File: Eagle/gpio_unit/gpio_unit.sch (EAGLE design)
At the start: 11 parts, among them X1 RASPI_GPIO_B+_PIN

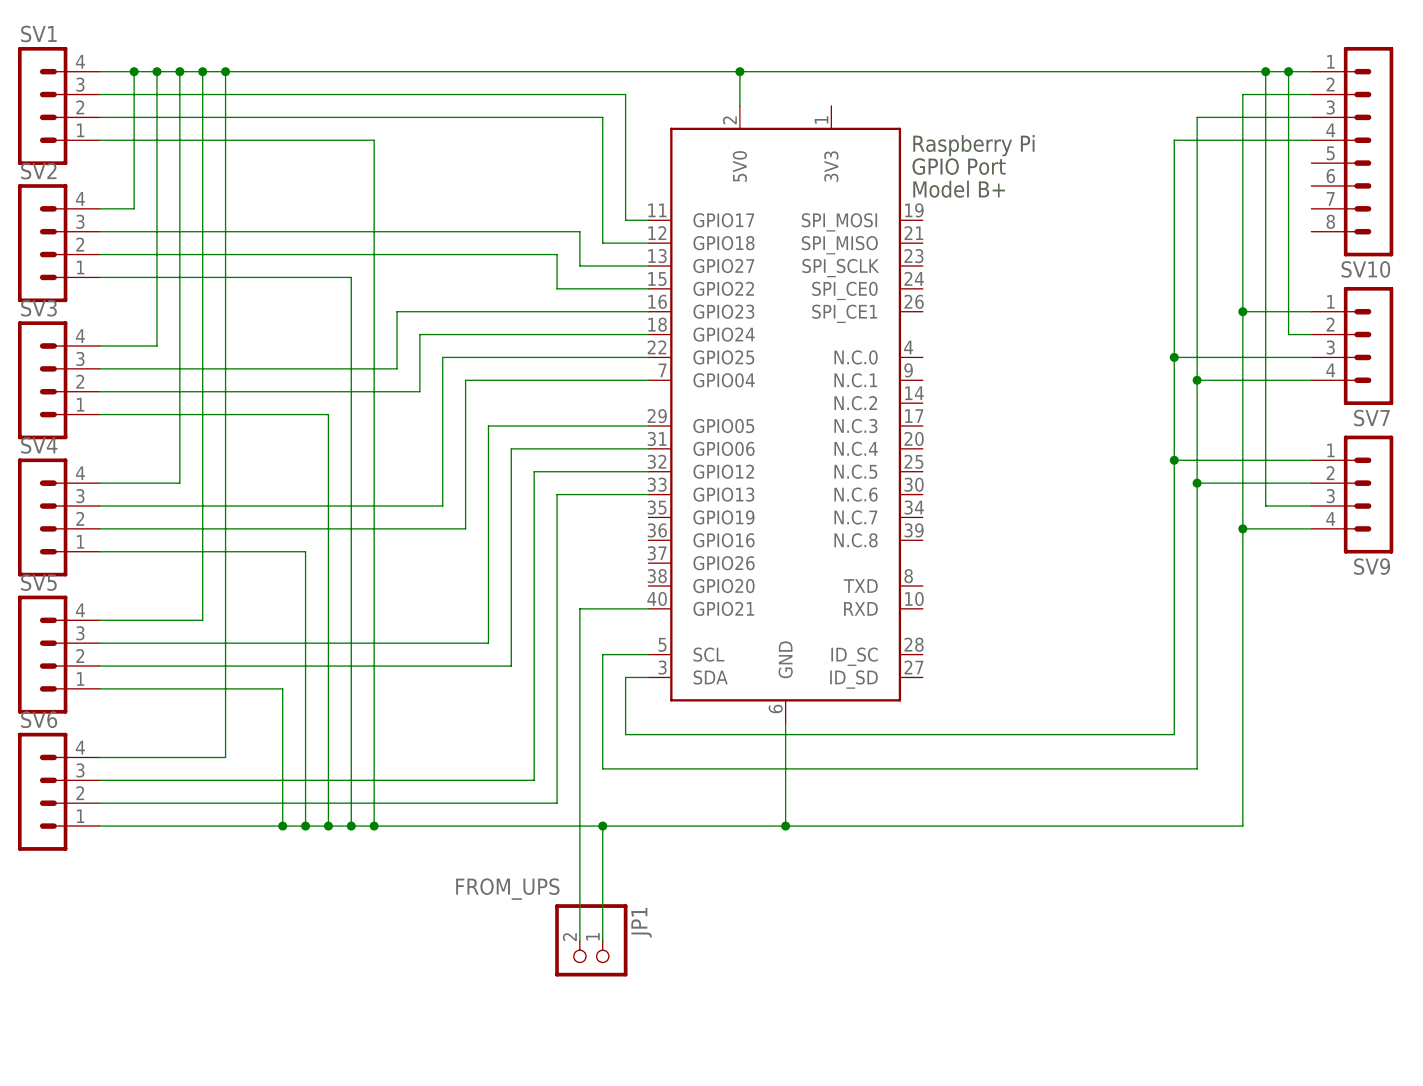
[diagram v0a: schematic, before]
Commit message: RPi GPIO unit
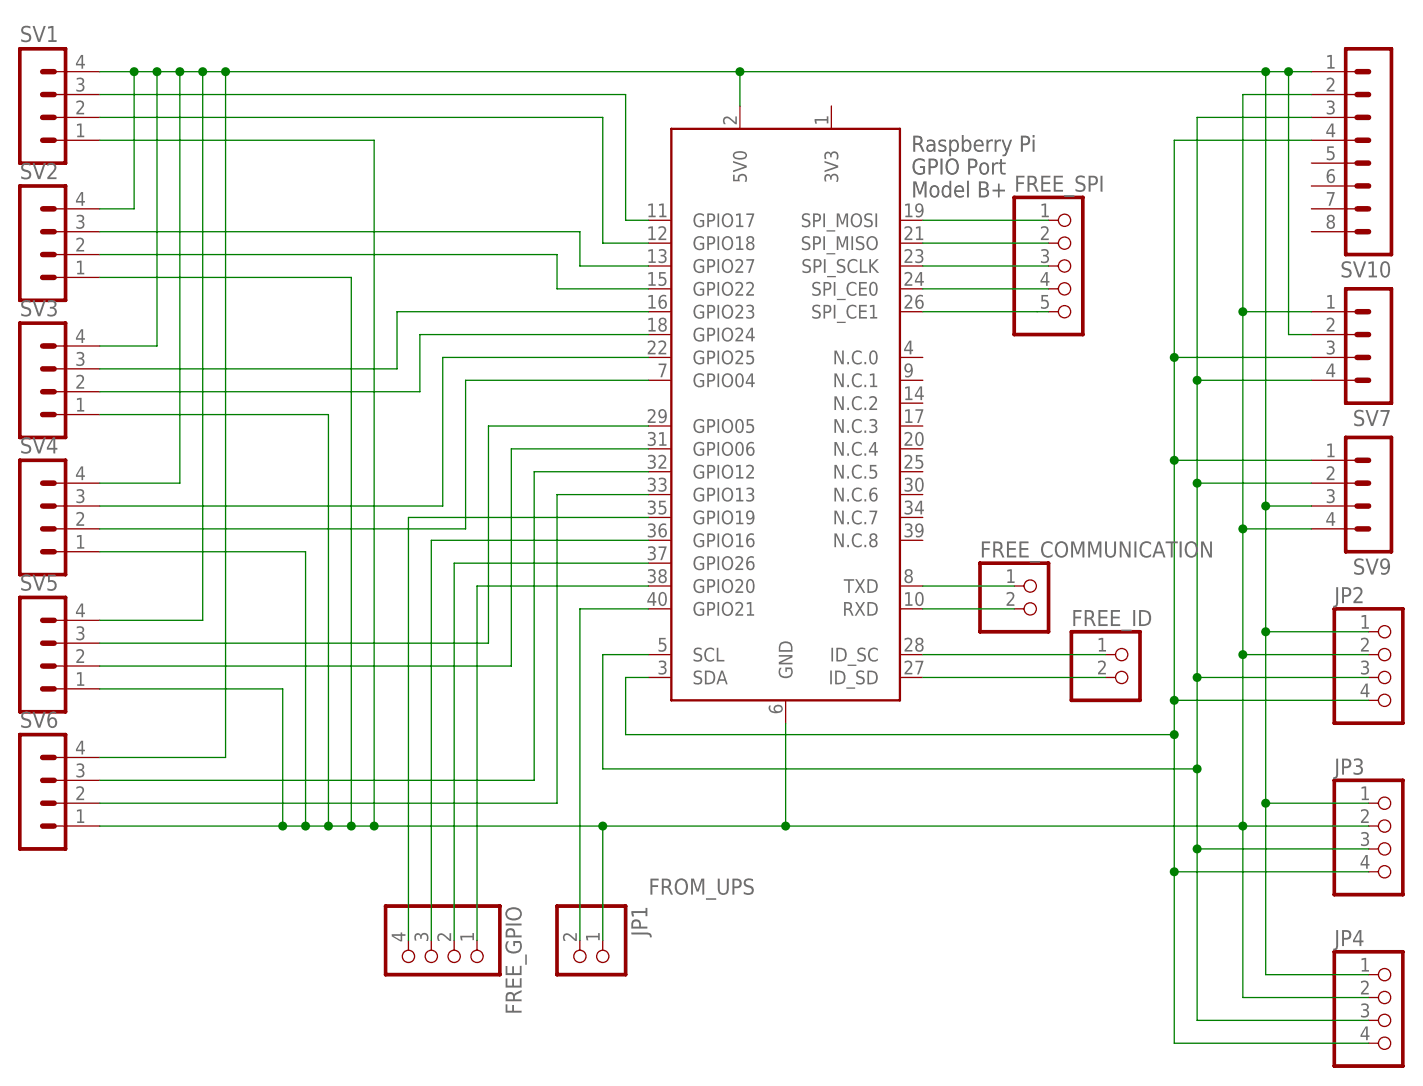
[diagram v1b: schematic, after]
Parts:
- added FREE_COMMUNICATION, FREE_ID: (no value), pinhead:PINHD-1X2/90
- added FREE_GPIO: (no value), pinhead:PINHD-1X4/90
- added FREE_SPI: (no value), pinhead:PINHD-1X5/90
- added JP2, JP3, JP4: (no value), pinhead:PINHD-1X4
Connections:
- new net N$16: FREE_SPI.1, X1.SPI_MOSI
- new net N$17: FREE_SPI.2, X1.SPI_MISO
- new net N$18: FREE_SPI.3, X1.SPI_SCLK
- new net N$19: FREE_SPI.4, X1.SPI_CE0
- new net N$20: FREE_SPI.5, X1.SPI_CE1
- new net N$21: FREE_COMMUNICATION.1, X1.TXD
- new net N$22: FREE_COMMUNICATION.2, X1.RXD
- new net N$23: FREE_ID.1, X1.ID_SC
- new net N$24: FREE_ID.2, X1.ID_SD
- new net N$25: FREE_GPIO.4, X1.GPIO19
- new net N$26: FREE_GPIO.3, X1.GPIO16
- new net N$27: FREE_GPIO.2, X1.GPIO26
- new net N$28: FREE_GPIO.1, X1.GPIO20
- net N$1: now also JP2.2, JP3.2, JP4.2
- net N$15: now also JP2.4, JP3.4, JP4.4
- net N$5: now also JP2.3, JP3.3, JP4.3
- net VDD: now also JP2.1, JP3.1, JP4.1
